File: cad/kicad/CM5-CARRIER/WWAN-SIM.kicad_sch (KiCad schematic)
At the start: 18 parts, among them J701 WWAN_M2_B_KEY_USB3_USB2, J702 693043020611, J703 693043020611, J711 CELL_1_RF, J712 CELL_2_RF, J713 CELL_3_RF, J714 CELL_4_GNSS_RF, J720 WWAN_CONTROL_TEST, U702 TPD4E05U06DQA, U703 TPD4E05U06DQA, U704 FSA2567MPX, U705 TPD4E05U06DQA, U706 TPD4E05U06DQA

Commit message: Complete A1 detailed carrier and audio capture
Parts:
- removed C701: 1000uF low-ESR, symbol Device:C
- removed C702: 100uF, symbol Device:C
- removed J702: 693043020611, CM5Carrier:J_Wurth_WR-CRD_693043020611, symbol CM5Carrier:Wurth_Nano_SIM_693043020611
- removed J720: WWAN_CONTROL_TEST, symbol Connector_Generic:Conn_02x06_Odd_Even
- removed U703, U706: TPD4E05U06DQA, symbol Power_Protection:TPD4E05U06DQA
- added C703: 10uF 25V X5R, Capacitor_SMD:C_0603_1608Metric, symbol Device:C
- added TP7201: MODEM_FULL_CARD_POWER_OFF_N, TestPoint:TestPoint_Pad_D2.0mm, symbol Connector:TestPoint
- added TP7202: MODEM_W_DISABLE1_N, TestPoint:TestPoint_Pad_D2.0mm, symbol Connector:TestPoint
- added TP7203: MODEM_RESET_N, TestPoint:TestPoint_Pad_D2.0mm, symbol Connector:TestPoint
- added TP7204: MODEM_WAKE_N, TestPoint:TestPoint_Pad_D2.0mm, symbol Connector:TestPoint
- added TP7205: MODEM_STATUS_LED_N, TestPoint:TestPoint_Pad_D2.0mm, symbol Connector:TestPoint
- added TP7206: MODEM_SIM_MUX_SEL_OD, TestPoint:TestPoint_Pad_D2.0mm, symbol Connector:TestPoint
- added TP7207: MODEM_3V8, TestPoint:TestPoint_Pad_D2.0mm, symbol Connector:TestPoint
- added TP7208: GND, TestPoint:TestPoint_Pad_D2.0mm, symbol Connector:TestPoint
- added U705, U706: TPD3F303DPV, Package_SON:Texas_R-PUSON-N8_USON-8-1EP_1.6x2.1mm_P0.5mm_EP0.4x1.7mm, symbol Power_Protection:TPD3F303DPV
- C704: footprint (none) -> Capacitor_SMD:C_0402_1005Metric; MPN (none) -> C1005X7R1H104K050BB; Manufacturer (none) -> TDK
- J702: renamed from U705; value TPD4E05U06DQA -> 693043020611; footprint (none) -> CM5Carrier:J_Wurth_WR-CRD_693043020611; symbol Power_Protection:TPD4E05U06DQA -> CM5Carrier:Wurth_Nano_SIM_693043020611; MPN TPD4E05U06DQAR -> 693043020611; Manufacturer Texas Instruments -> Wurth Elektronik
- J711, J712, J713, J714: MPN Final bulkhead MPN TBD -> 818033349; Manufacturer Amphenol RF / TE equivalent -> ECT
- R701: footprint (none) -> Resistor_SMD:R_0603_1608Metric; MPN (none) -> RC0603FR-07100KL; Manufacturer (none) -> Yageo
- U702: footprint (none) -> Package_SON:USON-10_2.5x1.0mm_P0.5mm
- U703: renamed from C703; value 10uF -> TPD4E05U06DQA; footprint (none) -> Package_SON:USON-10_2.5x1.0mm_P0.5mm; symbol Device:C -> Power_Protection:TPD4E05U06DQA; MPN (none) -> TPD4E05U06DQAR; Manufacturer (none) -> Texas Instruments
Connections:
- net CHASSIS_GND: now also J702.S1 (SHIELD), J702.S2 (SHIELD), J702.S3 (SHIELD), J702.S4 (SHIELD), J702.S5 (SHIELD), J702.S6 (SHIELD)
- net GND: now also J702.C5 (GND), U703.3 (GND), U703.8 (GND), C703.2, TP7208.1, U705.9 (GND), U706.9 (GND); no longer J702.3 (GND), J702.8 (GND), U703.2
- net MODEM_3V8: now also C703.1, TP7207.1; no longer U703.1
- net MODEM_FULL_CARD_POWER_OFF_N: now also TP7201.1
- net MODEM_RESET_N: now also TP7203.1
- net MODEM_SIM_MUX_SEL_OD: now also TP7206.1
- net MODEM_STATUS_LED_N: now also TP7205.1
- net MODEM_WAKE_N: now also TP7204.1
- net MODEM_W_DISABLE1_N: now also TP7202.1
- net SIM1_CLK: now also J702.C3 (CLOCK), U705.2 (CLK_OUT); no longer J702.4 (D2+), U704.9 (1CLK)
- net SIM1_DATA: now also J702.C7 (I/O), U705.1 (DATA1_OUT); no longer J702.5 (D2-), U704.13 (1DAT)
- net SIM1_RESET: now also J702.C2 (RESET), U705.3 (DATA2_OUT); no longer J702.2 (D1-), U704.5 (1RST)
- net SIM1_VCC: now also J702.C1 (VCC), U704.15 (2VSIM), U705.5 (V_{CC}); no longer J702.1 (D1+), U704.1 (1VSIM)
- net SIM2_CLK: now also U706.2 (CLK_OUT); no longer U704.7 (2CLK)
- net SIM2_DATA: now also U706.1 (DATA1_OUT); no longer U704.11 (2DAT)
- net SIM2_RESET: now also U706.3 (DATA2_OUT); no longer U704.3 (2RST)
- net SIM2_VCC: now also U704.1 (1VSIM), U706.5 (V_{CC}); no longer U704.15 (2VSIM)
- net WWAN_USB3_RX_N: now also U703.2 (D1-)
- net WWAN_USB3_RX_P: now also U703.1 (D1+)
- new net SIM1_CLK_RAW: U704.7 (2CLK), U705.7 (CLK_IN)
- new net SIM1_DATA_RAW: U704.11 (2DAT), U705.8 (DATA1_IN)
- new net SIM1_RESET_RAW: U704.3 (2RST), U705.6 (DATA2_IN)
- new net SIM2_CLK_RAW: U704.9 (1CLK), U706.7 (CLK_IN)
- new net SIM2_DATA_RAW: U704.13 (1DAT), U706.8 (DATA1_IN)
- new net SIM2_RESET_RAW: U704.5 (1RST), U706.6 (DATA2_IN)
- no-connect marks 57 -> 51
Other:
- note added: "Four off-board ECT 818033349 USS RF IV-to-SMA bulkhead pigtails; final cable length remains a routed sample gate."
- note added: "Physical SIM 1 uses FSA2567 channel 2 and physical SIM 2 uses channel 1 to implement that default."
- note added: "Power-Regulators C1189-C1192 provide 1320 uF low-ESR bulk beside the socket; C703/C704 are local HF bypass."
- note added: "SIM1: TPD3F303 filters RESET/CLK/DATA and clamps VCC beside the holder; shell bonds to CHASSIS_GND."
- note added: "SIM2: TPD3F303 filters RESET/CLK/DATA and clamps VCC beside the holder; shell bonds to CHASSIS_GND."
- note added: "TP7201-TP7208 are copper factory probes. USB 2/3 has no branch or generic test header."
- note removed: "Bulk values are the placement baseline; validate rail droop with the final global modem's burst-current profile."
- note removed: "Four short module U.FL/MHF pigtails terminate at the narrow right-side panel bulkheads; keep clear of PSU and fan motors."
- note removed: "J720 is a DNP factory test footprint, not a top-panel connector."
- note removed: "SIM1: ESD array adjacent to holder; electrical C5 to GND, metal shell to CHASSIS_GND."
- note removed: "SIM2: ESD array adjacent to holder; electrical C5 to GND, metal shell to CHASSIS_GND."

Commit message: Audit schematic logic against controlled datasheets
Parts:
- added C701, C702: 220uF 6.3V polymer, Capacitor_SMD:CP_Elec_8x6.9, symbol Device:C
- added C705, C708: 220pF C0G, Capacitor_SMD:C_0402_1005Metric, symbol Device:C
- added C706, C709: 68pF C0G, Capacitor_SMD:C_0402_1005Metric, symbol Device:C
- added C707: 100nF, Capacitor_SMD:C_0402_1005Metric, symbol Device:C
- added C710: 15pF C0G, Capacitor_SMD:C_0402_1005Metric, symbol Device:C
- added C711: 9.1pF C0G, Capacitor_SMD:C_0402_1005Metric, symbol Device:C
- added C712: 4.7pF C0G, Capacitor_SMD:C_0402_1005Metric, symbol Device:C
- added D701: 5.0V TVS, Diode_SMD:D_SOD-123F, symbol Device:D_TVS
- C703: value 10uF 25V X5R -> 100nF; footprint Capacitor_SMD:C_0603_1608Metric -> Capacitor_SMD:C_0402_1005Metric; MPN GRM188R61E106MA73D -> C1005X7R1H104K050BB; Manufacturer Murata -> TDK
- C704: value 100nF -> 6.8nF C0G; footprint Capacitor_SMD:C_0402_1005Metric -> Capacitor_SMD:C_0603_1608Metric; MPN C1005X7R1H104K050BB -> GRM1885C1H682JA01D; Manufacturer TDK -> Murata
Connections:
- net CHASSIS_GND: no longer J711.2 (Ext), J712.2 (Ext), J713.2 (Ext), J714.2 (Ext)
- net GND: now also C701.2, C702.2, C705.2, C706.2, C707.2, C708.2, C709.2, C710.2, C711.2, C712.2, D701.2 (A2)
- net MODEM_3V8: now also C701.1, C702.1, C705.1, C706.1, C707.1, C708.1, C709.1, C710.1, C711.1, C712.1, D701.1 (A1)
- net CELL_1_RF: no longer names the net of J711.1 (In)
- net CELL_2_RF: no longer names the net of J712.1 (In)
- net CELL_3_RF: no longer names the net of J713.1 (In)
- net CELL_4_GNSS_RF: no longer names the net of J714.1 (In)
- no-connect marks 51 -> 59
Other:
- note added: "C701-C712 and D701 implement the RM520N-GL two-bank VCC reference network directly at M.2 pins 2/4 and 70/72/74."
- note added: "Power-Regulators C1189-C1192 retain 1320 uF upstream bulk; they do not replace the socket-local 2 x 220 uF and HF ladder."
- note removed: "Power-Regulators C1189-C1192 provide 1320 uF low-ESR bulk beside the socket; C703/C704 are local HF bypass."

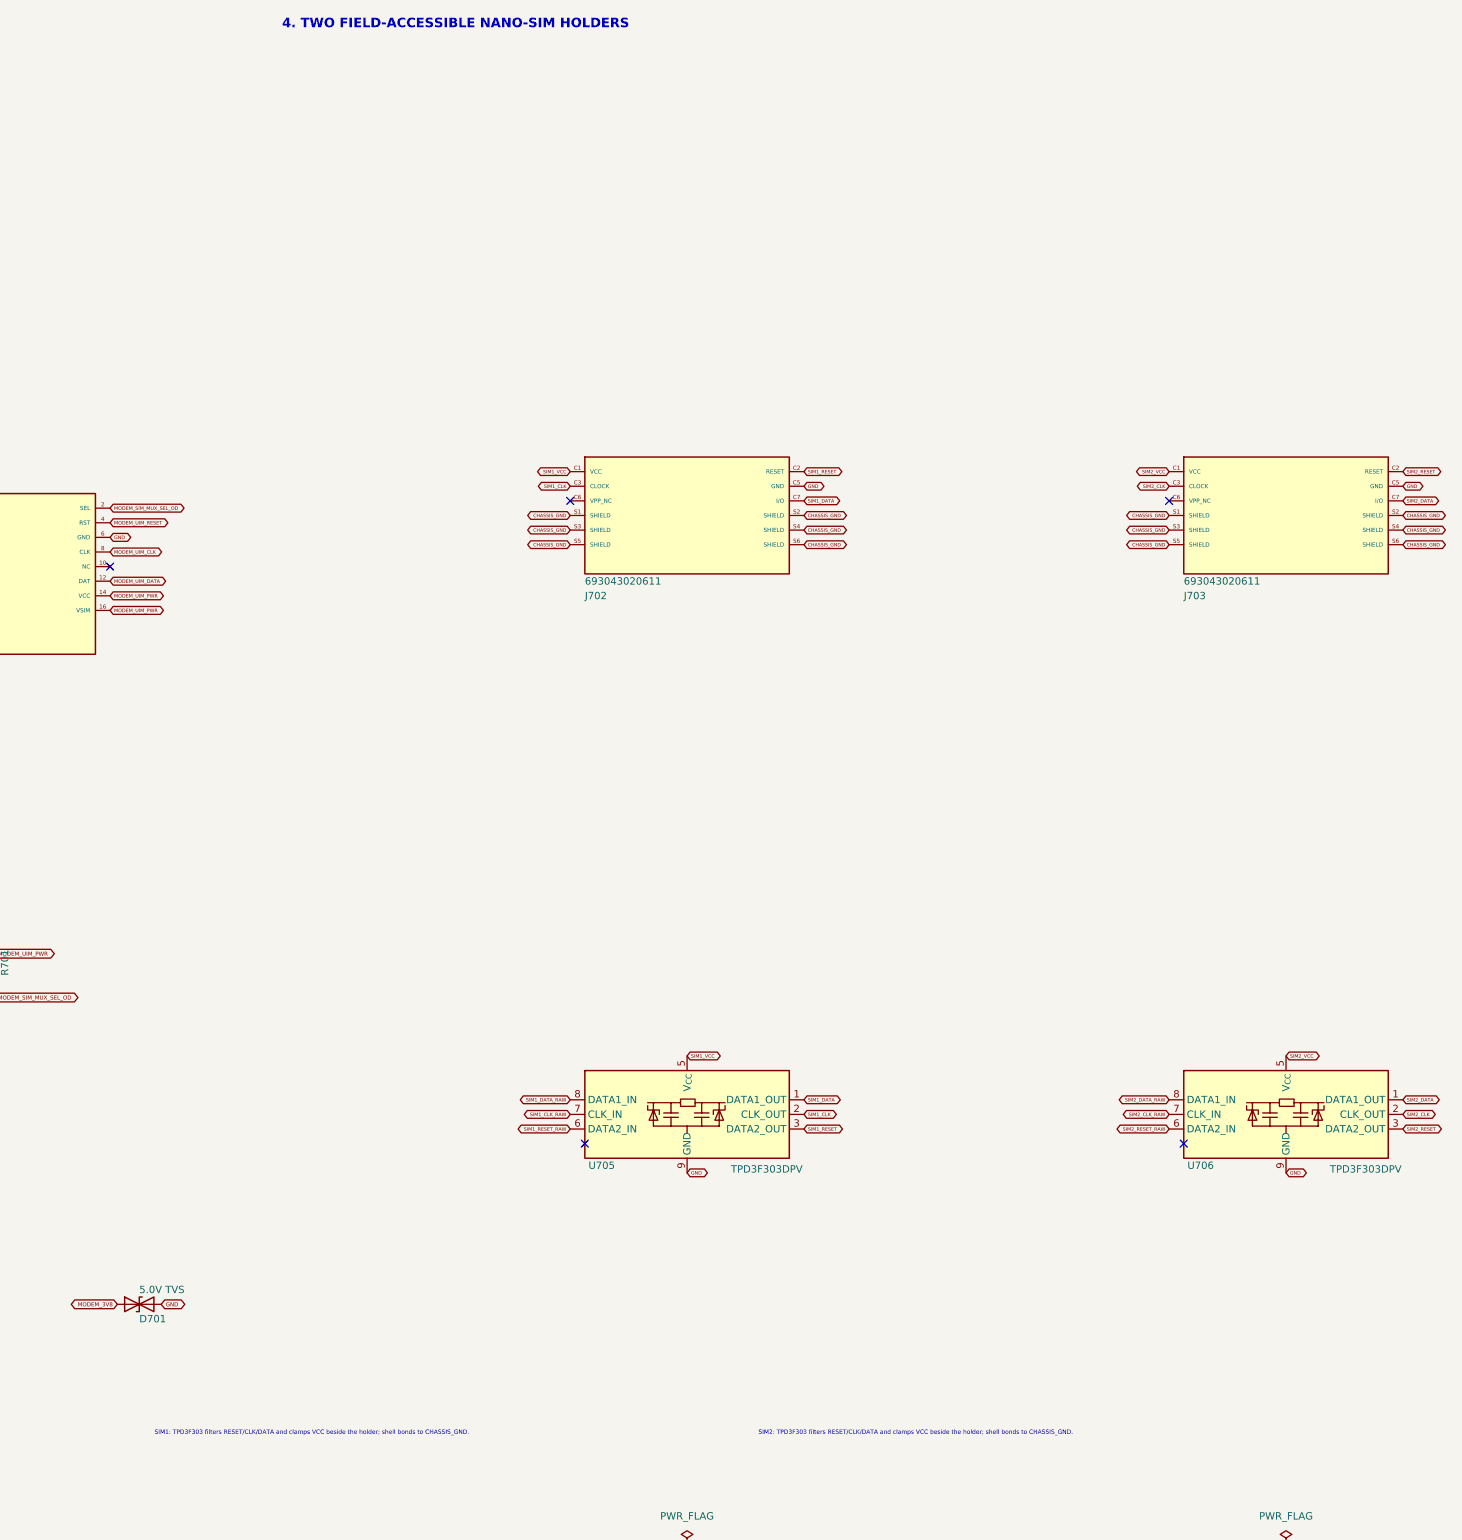
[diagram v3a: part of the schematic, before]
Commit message: Implement direct socketed dual-SIM daughterboard
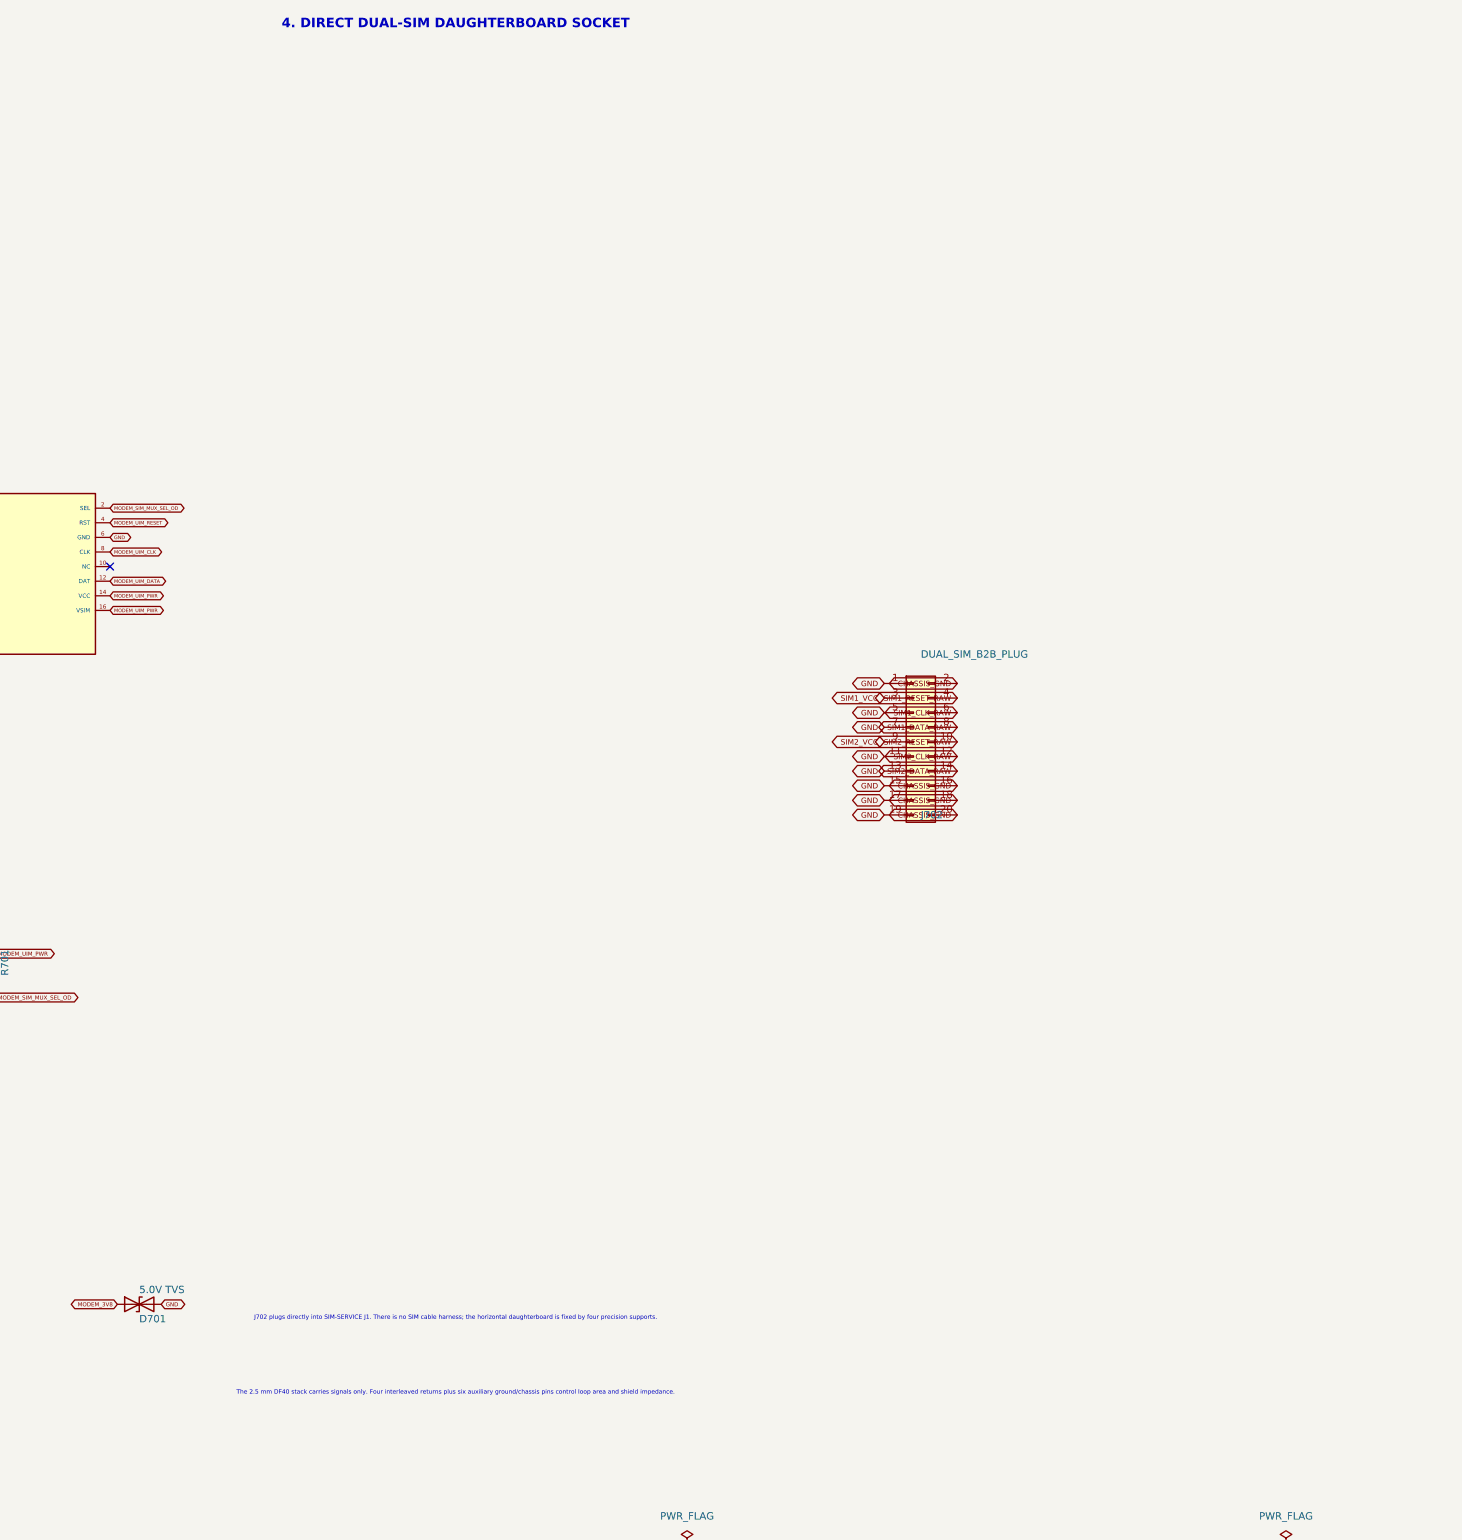
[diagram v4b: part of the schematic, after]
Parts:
- removed C703: 100nF, Capacitor_SMD:C_0402_1005Metric, symbol Device:C
- removed J702, J703: 693043020611, CM5Carrier:J_Wurth_WR-CRD_693043020611, symbol CM5Carrier:Wurth_Nano_SIM_693043020611
- removed U702, U703: TPD4E05U06DQA, Package_SON:USON-10_2.5x1.0mm_P0.5mm, symbol Power_Protection:TPD4E05U06DQA
- removed U705, U706: TPD3F303DPV, Package_SON:Texas_R-PUSON-N8_USON-8-1EP_1.6x2.1mm_P0.5mm_EP0.4x1.7mm, symbol Power_Protection:TPD3F303DPV
- added C712: 4.7pF C0G, Capacitor_SMD:C_0402_1005Metric, symbol Device:C
- added J702: DUAL_SIM_B2B_PLUG, CM5Carrier:Hirose_DF40C-20DP-0.4V_2x10-1MP_P0.4mm, symbol Connector_Generic:Conn_02x10_Odd_Even
- added R701: 100k, Resistor_SMD:R_0603_1608Metric, symbol Device:R
- added U704: FSA2567MPX, Package_DFN_QFN:WQFN-16-1EP_3x3mm_P0.5mm_EP1.68x1.68mm, symbol CM5Carrier:FSA2567MPX
- C703: renamed from R701; value 100k -> 100nF; footprint Resistor_SMD:R_0603_1608Metric -> Capacitor_SMD:C_0402_1005Metric; symbol Device:R -> Device:C; MPN RC0603FR-07100KL -> C1005X7R1H104K050BB; Manufacturer Yageo -> TDK
- U702: renamed from C712; value 4.7pF C0G -> TPD4E05U06DQA; footprint Capacitor_SMD:C_0402_1005Metric -> Package_SON:USON-10_2.5x1.0mm_P0.5mm; symbol Device:C -> Power_Protection:TPD4E05U06DQA; MPN GRM1555C1H4R7BA01D -> TPD4E05U06DQAR; Manufacturer Murata -> Texas Instruments
- U703: renamed from U704; value FSA2567MPX -> TPD4E05U06DQA; footprint Package_DFN_QFN:WQFN-16-1EP_3x3mm_P0.5mm_EP1.68x1.68mm -> Package_SON:USON-10_2.5x1.0mm_P0.5mm; symbol CM5Carrier:FSA2567MPX -> Power_Protection:TPD4E05U06DQA; MPN FSA2567MPX -> TPD4E05U06DQAR; Manufacturer onsemi -> Texas Instruments
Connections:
- net CHASSIS_GND: now also J702.16 (Pin_16), J702.18 (Pin_18), J702.2 (Pin_2), J702.20 (Pin_20)
- net GND: now also C703.2, U702.3 (GND), U702.8 (GND), U703.3 (GND), U703.8 (GND), C712.2, J702.1 (Pin_1), J702.11 (Pin_11), J702.13 (Pin_13), J702.15 (Pin_15), J702.17 (Pin_17), J702.19 (Pin_19), J702.5 (Pin_5), J702.7 (Pin_7), U704.17 (EP), U704.6 (GND); no longer U702.2, U703.17 (EP), U703.6 (GND)
- net MODEM_3V8: now also C703.1, C712.1; no longer U702.1
- net MODEM_SIM_MUX_SEL_OD: now also R701.2, U704.2 (SEL); no longer C703.2, U703.2 (SEL)
- net MODEM_UIM_CLK: now also U704.8 (CLK); no longer U703.8 (CLK)
- net MODEM_UIM_DATA: now also U704.12 (DAT); no longer U703.12 (DAT)
- net MODEM_UIM_PWR: now also R701.1, U704.14 (VCC), U704.16 (VSIM); no longer C703.1, U703.14 (VCC), U703.16 (VSIM)
- net MODEM_UIM_RESET: now also U704.4 (RST); no longer U703.4 (RST)
- net SIM1_CLK_RAW: now also J702.6 (Pin_6), U704.7 (2CLK); no longer U703.7 (2CLK)
- net SIM1_DATA_RAW: now also J702.8 (Pin_8), U704.11 (2DAT); no longer U703.11 (2DAT)
- net SIM1_RESET_RAW: now also J702.4 (Pin_4), U704.3 (2RST); no longer U703.3 (2RST)
- net SIM1_VCC: now also J702.3 (Pin_3), U704.15 (2VSIM); no longer U703.15 (2VSIM)
- net SIM2_CLK_RAW: now also J702.12 (Pin_12), U704.9 (1CLK); no longer U703.9 (1CLK)
- net SIM2_DATA_RAW: now also J702.14 (Pin_14), U704.13 (1DAT); no longer U703.13 (1DAT)
- net SIM2_RESET_RAW: now also J702.10 (Pin_10), U704.5 (1RST); no longer U703.5 (1RST)
- net SIM2_VCC: now also J702.9 (Pin_9), U704.1 (1VSIM); no longer U703.1 (1VSIM)
- net WWAN_USB2_DM: now also U702.2 (D1-)
- net WWAN_USB2_DP: now also U702.1 (D1+)
- net WWAN_USB3_RX_N: now also U703.2 (D1-)
- net WWAN_USB3_RX_P: now also U703.1 (D1+)
- net WWAN_USB3_TX_N: now also U702.5 (D2-)
- net WWAN_USB3_TX_P: now also U702.4 (D2+)
- no-connect marks 59 -> 55
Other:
- note added: "4. DIRECT DUAL-SIM DAUGHTERBOARD SOCKET"
- note added: "J702 plugs directly into SIM-SERVICE J1. There is no SIM cable harness; the horizontal daughterboard is fixed by four precision supports."
- note added: "The 2.5 mm DF40 stack carries signals only. Four interleaved returns plus six auxiliary ground/chassis pins control loop area and shield impedance."
- note removed: "4. TWO FIELD-ACCESSIBLE NANO-SIM HOLDERS"
- note removed: "SIM1: TPD3F303 filters RESET/CLK/DATA and clamps VCC beside the holder; shell bonds to CHASSIS_GND."
- note removed: "SIM2: TPD3F303 filters RESET/CLK/DATA and clamps VCC beside the holder; shell bonds to CHASSIS_GND."
